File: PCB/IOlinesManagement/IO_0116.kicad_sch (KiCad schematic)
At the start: 224 parts, among them Q17 BC337, Q18 BC337, Q19 BC337, Q20 BC337, Q21 BC337, Q22 BC337, Q23 BC337, Q24 BC337, Q25 BC337, Q26 BC337, Q27 BC337, Q28 BC337, Q29 BC337, Q30 BC337, Q31 BC337, Q32 BC337, Q33 BC337, Q34 BC337, Q35 BC327, Q36 BC337, Q37 BC337, Q38 BC337, Q39 BC337, Q40 BC337, Q41 BC337, Q42 BC337, Q43 BC337, Q44 BC337, Q45 BC337, Q46 BC337, Q47 BC337, Q48 BC337, Q49 BC337, Q50 BC337, Q51 BC327, Q52 BC337, Q53 BC337, Q54 BC337, Q55 BC337, Q56 BC337, Q57 BC337, Q58 BC337, Q59 BC337, Q60 BC337, Q61 BC337, Q62 BC337, Q63 BC337, Q64 BC337, Q65 BC337, Q66 BC337, Q67 BC327, Q68 BC327, Q69 BC327, Q70 BC327, Q71 BC327, Q72 BC327, Q73 BC327, Q74 BC327, Q75 BC327, Q76 BC327, Q77 BC327, Q78 BC327, Q79 BC327, Q80 BC327

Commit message: Fingerprints assignment
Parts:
- C1, C10, C11, C12, C13, C14, C15, C16, C2, C3, C4, C5, C6, C7, C8, C9: footprint (none) -> Capacitor_THT:C_Disc_D4.3mm_W1.9mm_P5.00mm
- Q17, Q18, Q19, Q20, Q21, Q22, Q23, Q24, Q25, Q26, Q27, Q28, Q29, Q30, Q31, Q32, Q33, Q34, Q35, Q36, Q37, Q38, Q39, Q40, Q41, Q42, Q43, Q44, Q45, Q46, Q47, Q48, Q49, Q50, Q51, Q52, Q53, Q54, Q55, Q56, Q57, Q58, Q59, Q60, Q61, Q62, Q63, Q64, Q65, Q66, Q67, Q68, Q69, Q70, Q71, Q72, Q73, Q74, Q75, Q76, Q77, Q78, Q79, Q80: footprint Package_TO_SOT_THT:TO-92_Inline -> Package_TO_SOT_THT:TO-92_Inline_Wide
- R100, R101, R102, R103, R104, R105, R106, R107, R108, R109, R110, R111, R112, R113, R114, R115, R116, R117, R118, R119, R120, R121, R122, R123, R124, R125, R126, R127, R128, R129, R130, R131, R132, R133, R134, R135, R136, R137, R138, R139, R140, R141, R142, R143, R144, R145, R146, R147, R148, R149, R150, R151, R152, R153, R154, R155, R156, R157, R158, R159, R160, R17, R18, R19, R20, R21, R22, R23, R24, R25, R26, R27, R28, R29, R30, R31, R32, R33, R34, R35, R36, R37, R38, R39, R40, R41, R42, R43, R44, R45, R46, R47, R48, R49, R50, R51, R52, R53, R54, R55, R56, R57, R58, R59, R60, R61, R62, R63, R64, R65, R66, R67, R68, R69, R70, R71, R72, R73, R74, R75, R76, R77, R78, R79, R80, R81, R82, R83, R84, R85, R86, R87, R88, R89, R90, R91, R92, R93, R94, R95, R96, R97, R98, R99: footprint (none) -> Resistor_SMD:R_1206_3216Metric

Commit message: Component size reduction and fixes
- Some connection to GND has been fixed
- The biggest part of (THT) BC337 components has been replaced by (SMD) BC817
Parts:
- removed Q17, Q18, Q19, Q20, Q21, Q22, Q36, Q37, Q38, Q39, Q40, Q52, Q53, Q54, Q55, Q56: BC337, Package_TO_SOT_THT:TO-92_Inline_Wide, symbol Transistor_BJT:BC337
- added Q17, Q18, Q19, Q20, Q21, Q22, Q81, Q82, Q83, Q84, Q85, Q86, Q87, Q88, Q89, Q90: BC817, Package_TO_SOT_SMD:SOT-23, symbol Transistor_BJT:BC817
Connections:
- net GND: now also Q48.3 (E), Q17.2 (E), Q18.2 (E), Q19.2 (E), Q20.2 (E), Q21.2 (E), Q22.2 (E), Q81.2 (E), Q82.2 (E), Q83.2 (E), Q84.2 (E), Q85.2 (E), Q86.2 (E), Q87.2 (E), Q88.2 (E), Q89.2 (E), Q90.2 (E)
- net at Q26.2 (B), R28.2: now also Q81.3 (C)
- net at Q62.2 (B), R93.2: now also Q88.3 (C)
- net at Q48.2 (B), R67.2: now also Q20.3 (C)
- net at R54.2: now also Q20.1 (B)
- net at R21.2: now also Q19.1 (B)
- net at R51.2: now also Q85.1 (B)
- net at Q66.2 (B), R99.2: now also Q89.3 (C)
- net at R84.2: now also Q89.1 (B)
- net at R53.2: now also Q22.1 (B)
- net at R18.2: now also Q81.1 (B)
- net at Q32.2 (B), R37.2: now also Q19.3 (C)
- net at Q60.2 (B), R90.2: now also Q87.3 (C)
- net at Q58.2 (B), R87.2: now also Q86.3 (C)
- net at Q64.2 (B), R96.2: now also Q90.3 (C)
- net at Q44.2 (B), R61.2: now also Q84.3 (C)
- net at R52.2: now also Q84.1 (B)
- net at R80.2: now also Q86.1 (B)
- net at Q46.2 (B), R64.2: now also Q22.3 (C)
- net at R81.2: now also Q87.1 (B)
- net at Q30.2 (B), R34.2: now also Q82.3 (C)
- net at R19.2: now also Q18.1 (B)
- net at Q42.2 (B), R58.2: now also Q85.3 (C)
- net at Q34.2 (B), R40.2: now also Q83.3 (C)
- net at Q24.2 (B), R25.2: now also Q17.3 (C)
- net at R83.2: now also Q90.1 (B)
- net at Q48.1 (C): now also R74.2
- net at Q28.2 (B), R31.2: now also Q18.3 (C)
- net at R17.2: now also Q17.1 (B)
- net at R22.2: now also Q83.1 (B)
- net at Q50.2 (B), R70.2: now also Q21.3 (C)
- net at R55.2: now also Q21.1 (B)
- net at R20.2: now also Q82.1 (B)
- net at R82.2: now also Q88.1 (B)

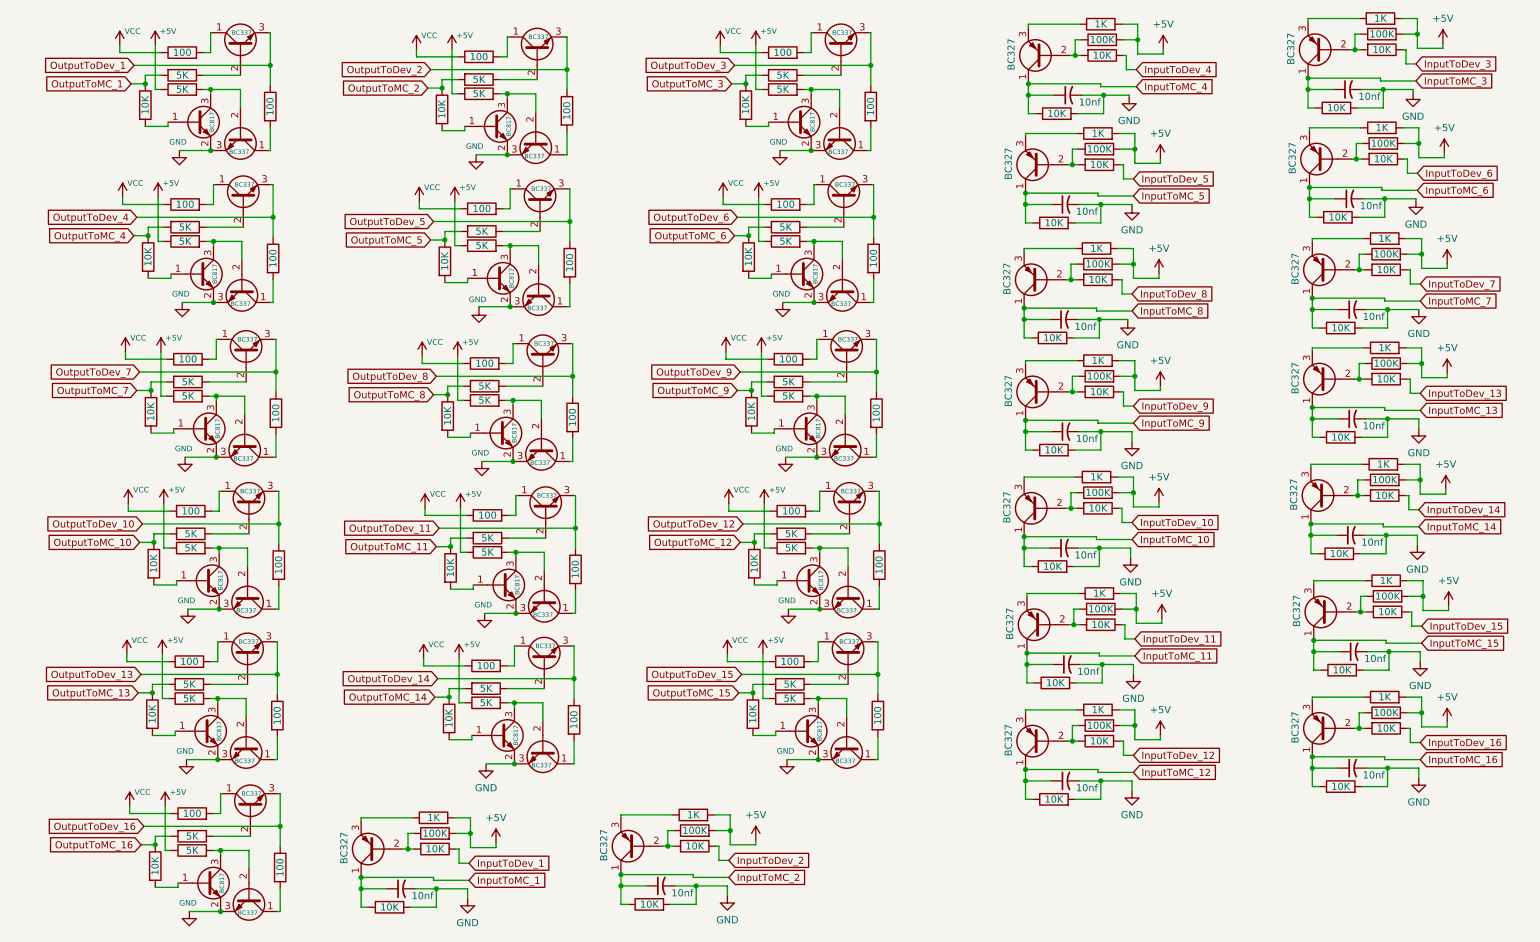
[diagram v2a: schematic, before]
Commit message: Changes: balanced push-pull architecture
At the beginning the idea was to allow the user to generate digital outputs with different formats.. (5, 12V..). In order
to achieve the result I used a customized push-pull structure with three NPN transistors. But that solution wastes a bit of
current and it not a good one, at the end. So, I have changed to a more common push-pull (PNP + NPN), but the output is not
connected to the transistors emitter, but to their collector, so the transistors work always on saturation area.
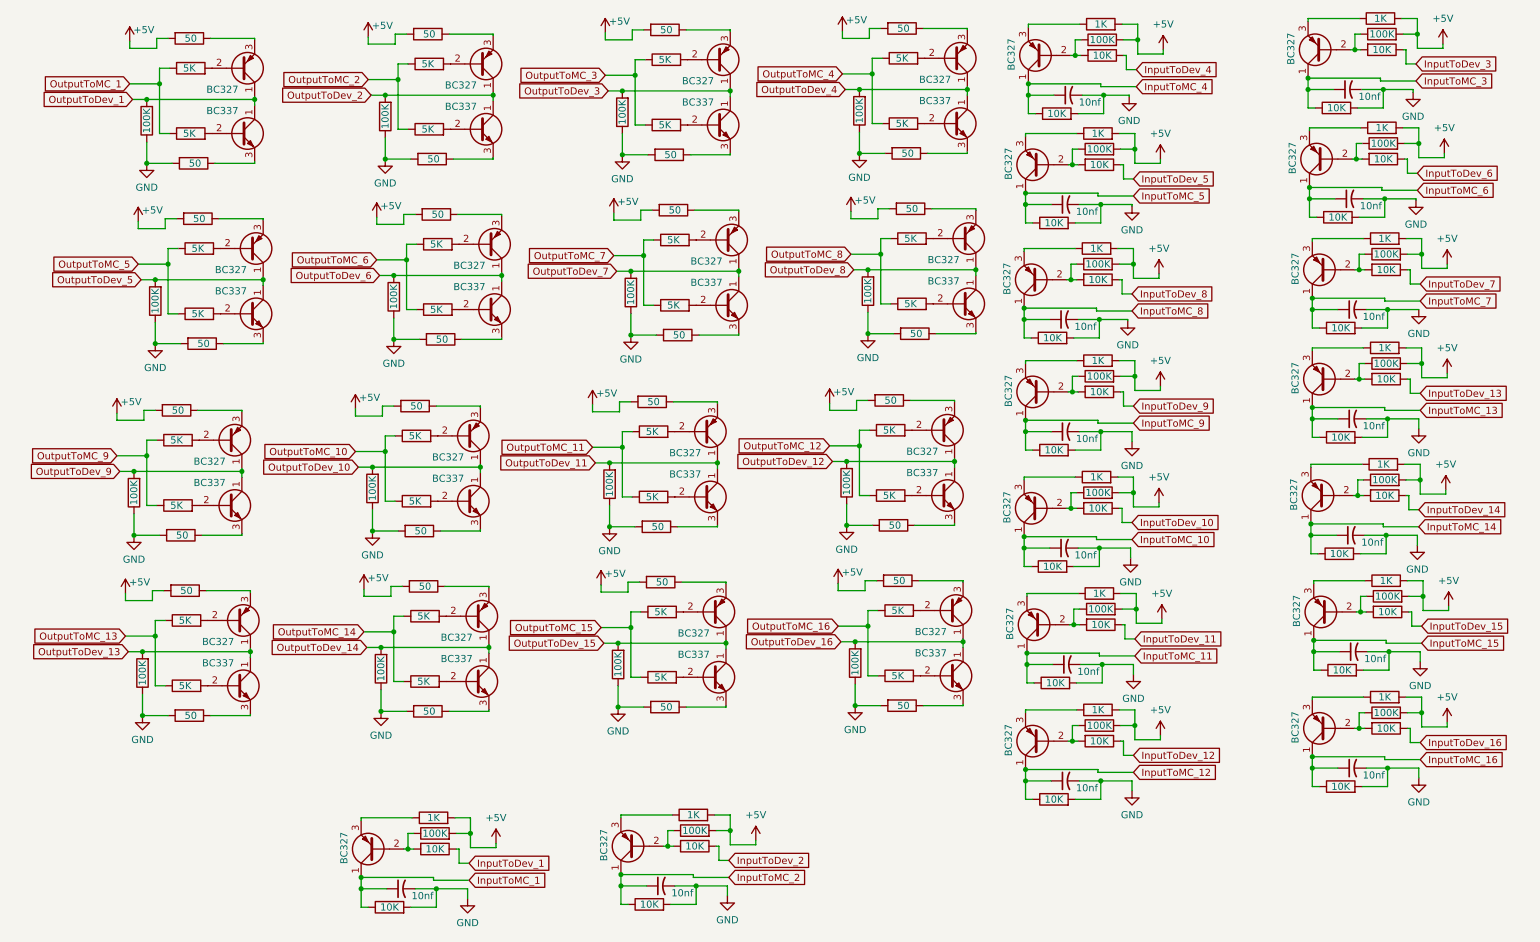
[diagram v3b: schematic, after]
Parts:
- removed Q17, Q18, Q19, Q20, Q21, Q22, Q81, Q82, Q83, Q84, Q85, Q86, Q87, Q88, Q89, Q90: BC817, Package_TO_SOT_SMD:SOT-23, symbol Transistor_BJT:BC817
- removed Q23, Q25, Q26, Q28, Q30, Q32, Q34, Q41, Q43, Q45, Q47, Q49, Q57, Q58, Q59, Q60, Q61, Q62, Q63, Q64, Q65, Q66: BC337, Package_TO_SOT_THT:TO-92_Inline_Wide, symbol Transistor_BJT:BC337
- removed R40: 5K, Resistor_SMD:R_1206_3216Metric, symbol Device:R
- removed R54, R55, R82, R83, R84: 10K, Resistor_SMD:R_1206_3216Metric, symbol Device:R
- removed R56, R65: 100, Resistor_SMD:R_1206_3216Metric, symbol Device:R
- added Q17, Q19, Q21, Q23, Q26, Q28, Q30, Q32, Q35, Q37, Q39, Q41, Q43, Q45, Q47, Q49: BC327, Package_TO_SOT_THT:TO-92_Inline_Wide, symbol Transistor_BJT:BC327
- added Q18, Q20, Q22, Q36, Q38, Q40: BC337, Package_TO_SOT_THT:TO-92_Inline_Wide, symbol Transistor_BJT:BC337
- added R47, R48, R76, R79: 5K, Resistor_SMD:R_1206_3216Metric, symbol Device:R
- added R49, R50, R77, R78: 50, Resistor_SMD:R_1206_3216Metric, symbol Device:R
- R100, R101, R104, R29, R32, R42, R45, R46, R73, R74, R97: value 100 -> 50
- R102, R103, R23, R26, R35, R43, R44, R59, R68, R71, R72, R75, R91, R94: value 100 -> 5K
- R17, R18, R19, R20: value 10K -> 100K
- R21, R53, R81: value 10K -> 50
- R22, R51, R52, R80: value 10K -> 5K
- R24, R25, R28, R33, R36, R57, R60, R66, R69, R70, R89, R92, R93, R96: value 5K -> 50
- R37, R39, R61, R63, R64, R86, R87: value 5K -> 100K
- R38, R41, R62, R85, R88: value 100 -> 100K
- renumbered Q35 to Q25, Q51 to Q34, Q67 to Q51, Q68 to Q52, Q69 to Q53, Q70 to Q54, Q71 to Q55, Q72 to Q56, Q73 to Q57, Q74 to Q58, Q75 to Q59, Q76 to Q60, Q77 to Q61, Q78 to Q62, Q79 to Q63, Q80 to Q64, R47 to R40, R48 to R54, R49 to R55, R50 to R56, R76 to R65, R77 to R82, R78 to R83, R79 to R84
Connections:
- net +5V: now also R101.2, R21.2, R25.2, R28.2, R33.2, R42.2, R46.2, R57.2, R66.2, R70.2, R73.2, R89.2, R93.2, R96.2, R49.2, R78.2; no longer R25.1, R28.1, R31.1, R34.1, R37.1, R58.1, R61.1, R64.1, R67.1, R70.1, R87.1, R90.1, R93.1, R96.1, R99.1
- net GND: now also R100.2, R104.2, R17.1, R18.1, R19.1, R20.1, R24.2, R29.2, R32.2, R36.2, R37.1, R38.1, R39.1, R41.1, R45.2, R53.2, R60.2, R61.1, R62.1, R63.1, R64.1, R69.2, R74.2, R81.2, R85.1, R86.1, R87.1, R88.1, R92.2, R97.2, R50.2, R77.2; no longer Q24.3 (E), Q42.3 (E), Q44.3 (E), Q46.3 (E), Q48.3 (E), Q50.3 (E)
- net OutputToDev_1: now also R19.2, Q21.1 (C), Q22.1 (C); no longer R41.1
- net OutputToDev_10: now also Q27.1 (C), R37.2, Q26.1 (C); no longer Q31.3 (E), R45.1
- net OutputToDev_11: now also R61.2, Q35.1 (C), Q36.1 (C); no longer R75.1
- net OutputToDev_12: now also Q44.1 (C), R85.2, Q43.1 (C); no longer R104.1
- net OutputToDev_13: now also R18.2, Q19.1 (C), Q20.1 (C); no longer Q29.3 (E), R44.1
- net OutputToDev_14: now also Q29.1 (C), R38.2, Q28.1 (C); no longer R74.1
- net OutputToDev_15: now also R62.2, Q37.1 (C), Q38.1 (C); no longer R103.1
- net OutputToDev_16: now also Q46.1 (C), R86.2, Q45.1 (C); no longer Q33.3 (E), R46.1
- net OutputToDev_2: now also Q31.1 (C), R39.2, Q30.1 (C); no longer R71.1
- net OutputToDev_3: now also R63.2, Q39.1 (C), Q40.1 (C); no longer R100.1
- net OutputToDev_4: now also Q48.1 (C), R87.2, Q47.1 (C); no longer R42.1
- net OutputToDev_5: now also Q24.1 (C), R20.2, Q23.1 (C); no longer R72.1
- net OutputToDev_6: now also Q33.1 (C), R41.2, Q32.1 (C); no longer R101.1
- net OutputToDev_7: now also Q42.1 (C), R64.2, Q41.1 (C); no longer Q27.3 (E), R43.1
- net OutputToDev_8: now also Q50.1 (C), R88.2, Q49.1 (C); no longer R73.1
- net OutputToDev_9: now also R17.2, Q17.1 (C), Q18.1 (C); no longer R102.1
- net OutputToMC_1: now also R30.1, R31.1; no longer R17.1, R24.2
- net OutputToMC_10: now also R43.1, R44.1; no longer R21.1, R36.2
- net OutputToMC_11: now also R67.1, R68.1; no longer R69.2
- net OutputToMC_12: now also R90.1, R91.1; no longer R98.2
- net OutputToMC_13: now also R26.1, R27.1; no longer R20.1, R33.2
- net OutputToMC_14: now also R47.1, R48.1; no longer R66.2
- net OutputToMC_15: now also R71.1, R72.1; no longer R95.2
- net OutputToMC_16: now also R94.1, R95.1; no longer R22.1, R39.2
- net OutputToMC_2: now also R52.1; no longer R57.2
- net OutputToMC_3: now also R75.1, R76.1; no longer R80.1, R86.2
- net OutputToMC_4: now also R98.1, R99.1; no longer R18.1, R27.2
- net OutputToMC_5: now also R34.1, R35.1; no longer R52.1, R60.2
- net OutputToMC_6: now also R58.1, R59.1; no longer R81.1, R89.2
- net OutputToMC_7: now also R80.1, R79.1; no longer R19.1, R30.2
- net OutputToMC_8: now also R102.1, R103.1; no longer R53.1, R63.2
- net OutputToMC_9: now also R22.1, R23.1; no longer R92.2
- net at R102.2: now also Q49.2 (B)
- net at R103.2: now also Q50.2 (B)
- net at R51.2: now also Q30.2 (B)
- net at R58.2: now also Q32.2 (B); no longer Q42.2 (B)
- net at R92.1: now also Q44.3 (E)
- net at R99.2: now also Q48.2 (B)
- net at R52.2: now also Q31.2 (B)
- net at Q44.2 (B): now also R91.2; no longer R61.2
- net at Q33.2 (B): now also R59.2; no longer R39.1
- net at R31.2: now also Q22.2 (B)
- net at R36.1: now also Q24.3 (E); no longer Q31.2 (B)
- net at R67.2: now also Q35.2 (B); no longer Q48.2 (B)
- net at R80.2: now also Q42.2 (B)
- net at R90.2: now also Q43.2 (B)
- net at R60.1: now also Q33.3 (E)
- net at R89.1: now also Q43.3 (E)
- net at R23.2: now also Q18.2 (B)
- net at R24.1: now also Q18.3 (E)
- net at R57.1: now also Q32.3 (E)
- net at R44.2: now also Q27.2 (B)
- net at R34.2: now also Q23.2 (B)
- net at R68.2: now also Q36.2 (B)
- net at R69.1: now also Q36.3 (E)
- net at R66.1: now also Q35.3 (E)
- net at R22.2: now also Q17.2 (B)
- net at R71.2: now also Q37.2 (B); no longer Q42.1 (C)
- net at Q24.2 (B): now also R35.2; no longer R25.2
- net at R94.2: now also Q45.2 (B)
- net at R26.2: now also Q19.2 (B)
- net at Q46.2 (B): now also R95.2; no longer R64.2
- net at R75.2: now also Q39.2 (B); no longer Q50.1 (C)
- net at R43.2: now also Q26.2 (B)
- net at R33.1: now also Q23.3 (E); no longer Q29.2 (B)
- net at R72.2: now also Q38.2 (B); no longer Q44.1 (C)
- removed net VCC: R23.1, R26.1, R29.1, R32.1, R35.1, R38.1, R59.1, R62.1, R68.1, R85.1, R88.1, R91.1, R94.1, R97.1
- new net: Q30.3 (E), R49.1
- new net: Q26.3 (E), R42.1
- new net: Q39.3 (E), R73.1
- new net: Q21.2 (B), R30.2
- new net: Q40.3 (E), R77.1
- new net: Q47.2 (B), R98.2
- new net: Q37.3 (E), R70.1
- new net: Q20.2 (B), R27.2
- new net: Q20.3 (E), R29.1
- new net: Q48.3 (E), R100.1
- new net: Q21.3 (E), R28.1
- new net: Q50.3 (E), R104.1
- new net: Q46.3 (E), R97.1
- new net: Q29.3 (E), R50.1
- new net: Q31.3 (E), R53.1
- new net: Q22.3 (E), R32.1
- new net: Q17.3 (E), R21.1
- new net: Q41.2 (B), R79.2
- new net: Q42.3 (E), R81.1
- new net: Q28.2 (B), R47.2
- new net: Q47.3 (E), R96.1
- new net: Q27.3 (E), R45.1
- new net: Q40.2 (B), R76.2
- new net: Q49.3 (E), R101.1
- new net: Q19.3 (E), R25.1
- new net: Q28.3 (E), R46.1
- new net: Q41.3 (E), R78.1
- new net: Q45.3 (E), R93.1
- new net: Q38.3 (E), R74.1
- new net: Q29.2 (B), R48.2
